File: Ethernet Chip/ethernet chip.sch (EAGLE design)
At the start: 31 parts

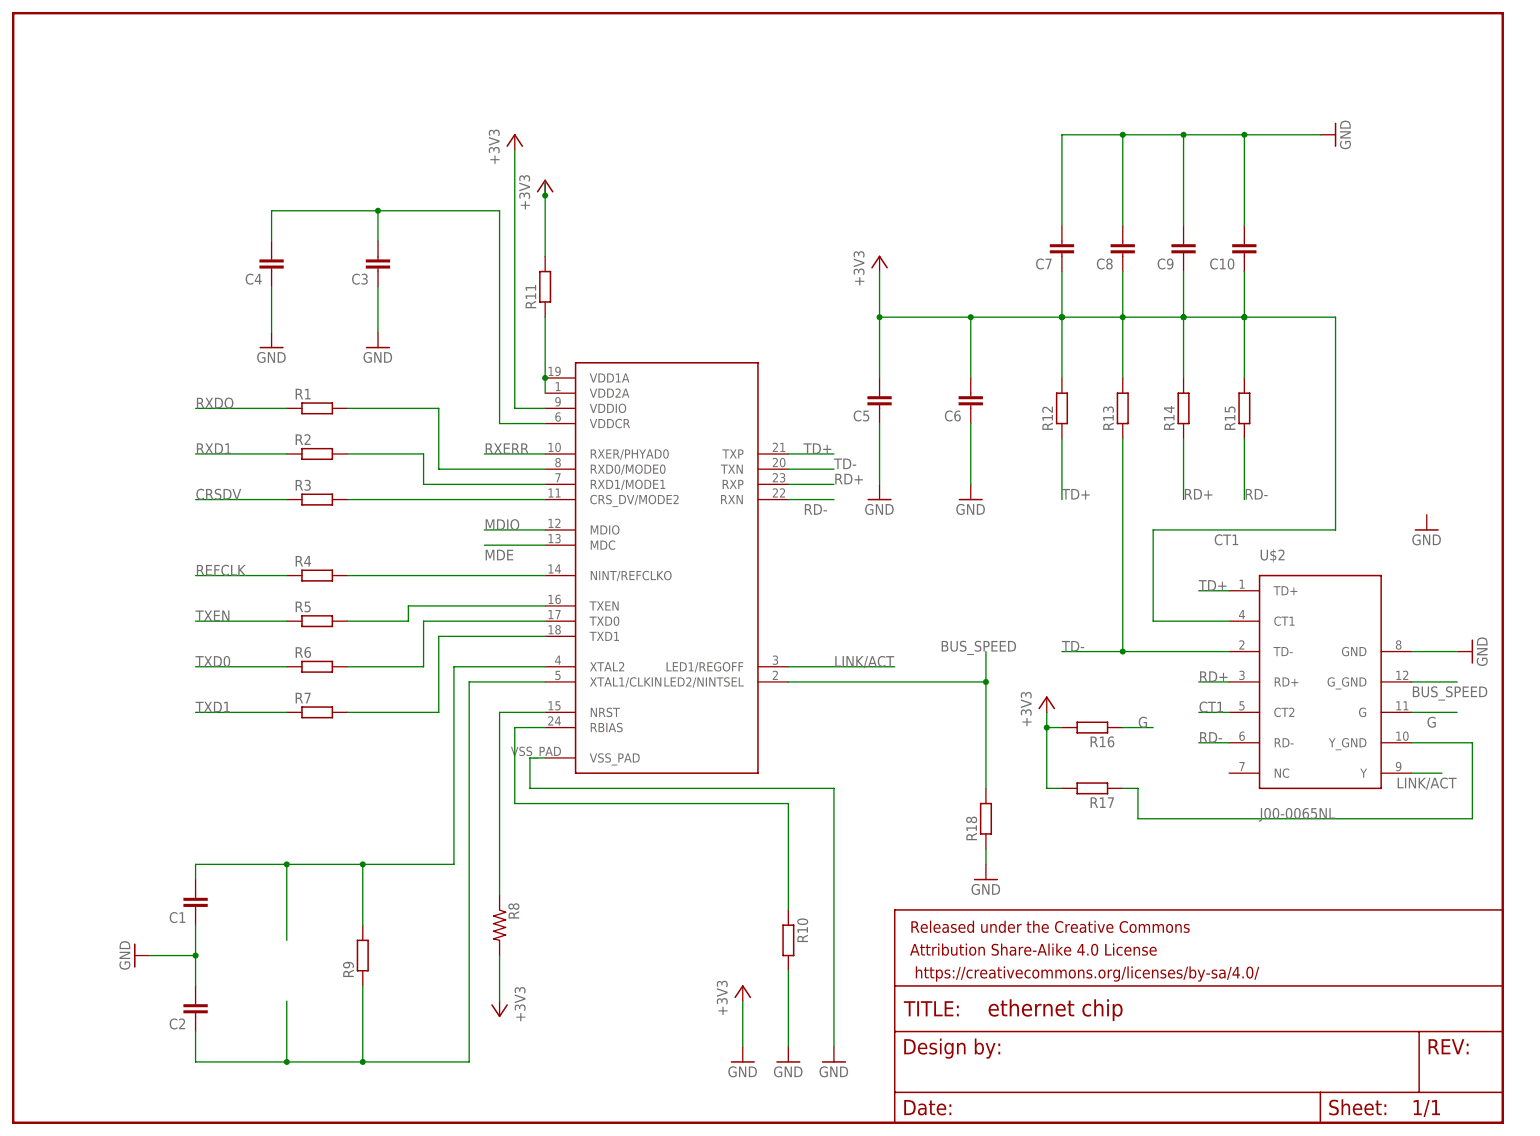
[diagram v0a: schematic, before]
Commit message: Updated Ethernet Schematic (From Paul)
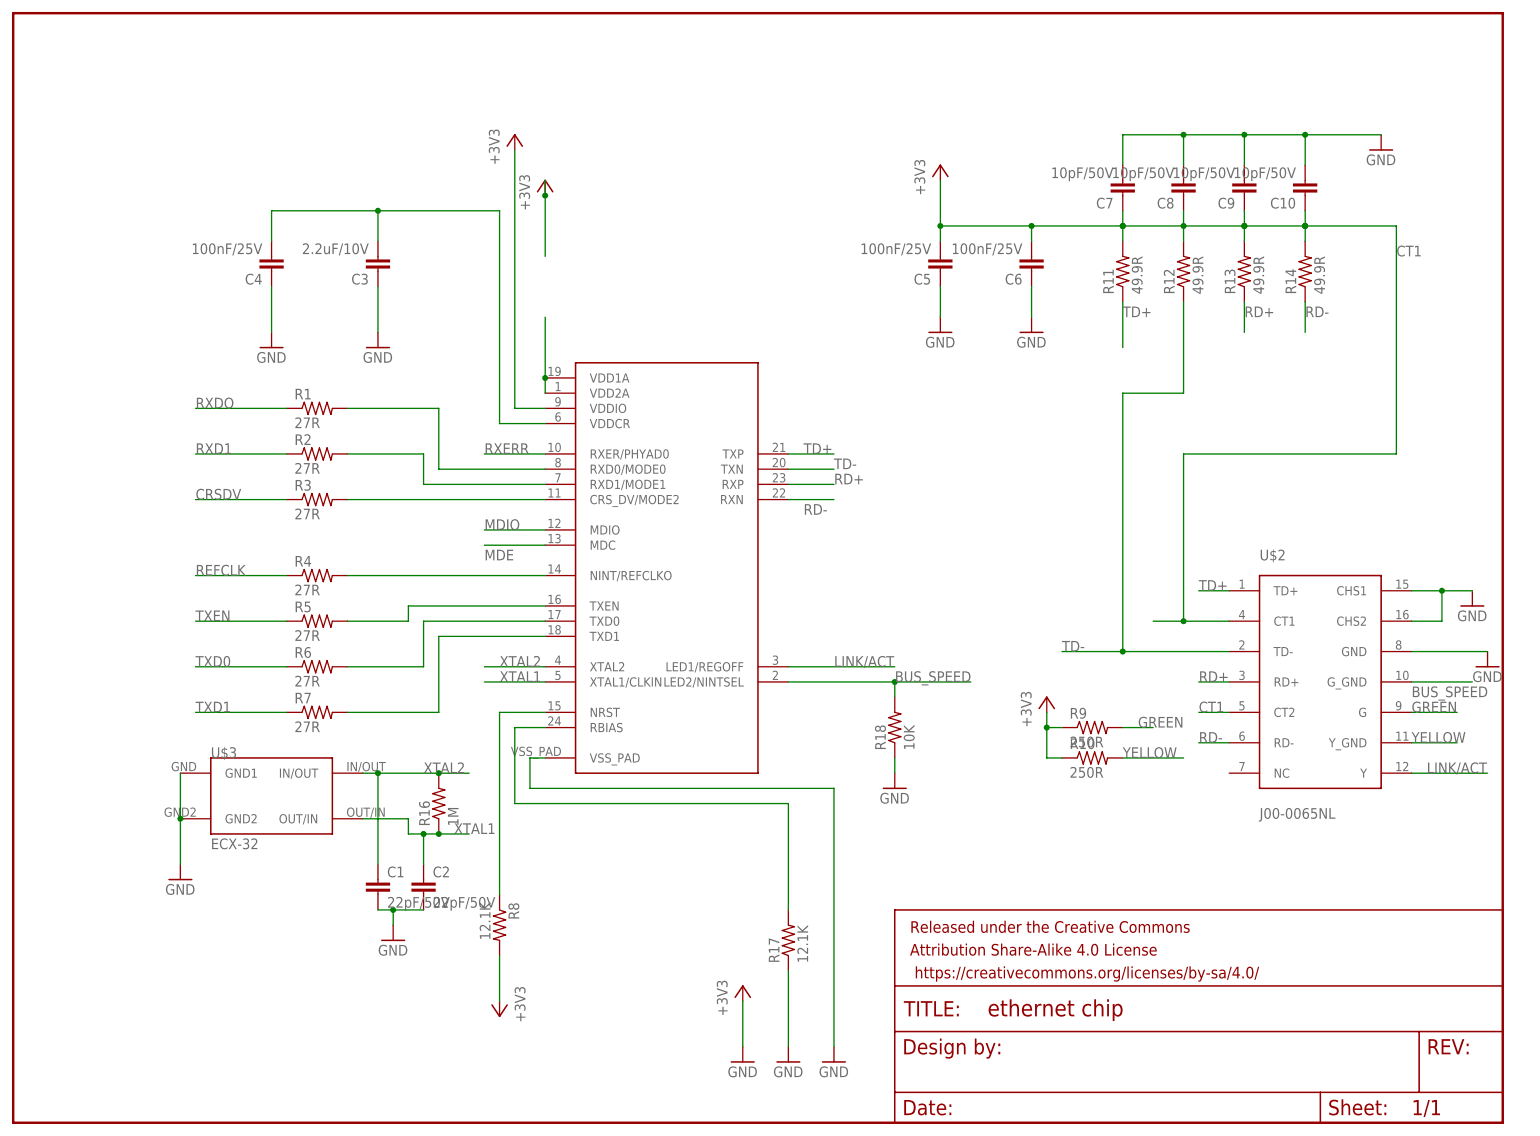
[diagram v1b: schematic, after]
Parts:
- removed R15: (no value), eagle-ltspice:RR0603
- added U$3: ECX-32, Other:ECX-32
- C1, C2: value (none) -> 22pF/50V
- C10, C7, C8, C9: value (none) -> 10pF/50V
- C3: value (none) -> 2.2uF/10V
- C4, C5, C6: value (none) -> 100nF/25V
- R1, R2, R3, R4, R5, R6, R7: value (none) -> 27R; device eagle-ltspice:RR0603 -> resistor:R-US_R0603
- R10, R9: value (none) -> 250R; device eagle-ltspice:RR0603 -> resistor:R-US_R0603
- R11, R12, R13, R14: value (none) -> 49.9R; device eagle-ltspice:RR0603 -> resistor:R-US_R0603
- R16: value (none) -> 1M; device eagle-ltspice:RR0603 -> resistor:R-US_R0603
- R17: value (none) -> 12.1K; device eagle-ltspice:RR0603 -> resistor:R-US_R0603
- R18: value (none) -> 10K; device eagle-ltspice:RR0603 -> resistor:R-US_R0603
- R8: value (none) -> 12.1K
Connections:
- removed net G: R16.1, U$2.G
- removed net N$12: C1.2, R9.2, U$1.XTAL2
- removed net N$13: C2.1, R9.1, U$1.XTAL1/CLKIN
- removed net N$18: R17.1, U$2.Y_GND
- new net GREEN: R9.2, U$2.G
- new net XTAL1: C2.1, R16.1, U$1.XTAL1/CLKIN, U$3.OUT/IN
- new net XTAL2: C1.1, R16.2, U$1.XTAL2, U$3.IN/OUT
- new net YELLOW: R10.2, U$2.Y_GND
- net +3V3: now also R10.1, R9.1; no longer R11.2, R16.2, R17.2
- net CT1: now also R11.2; no longer R15.2
- net GND: now also C1.2, R17.1, U$2.CHS1, U$2.CHS2, U$3.GND1, U$3.GND2; no longer C1.1, R10.2
- net N$11: no longer R11.1
- net N$4: now also R17.2; no longer R10.1
- net RD+: now also R13.1; no longer R14.1
- net RD-: now also R14.1; no longer R15.1
- net TD+: now also R11.1; no longer R12.1
- net TD-: now also R12.1; no longer R13.1
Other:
- moved on the sheet: C1, C10, C2, C5, C6, C7, C8, C9

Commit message: Cleaned up microboard folder
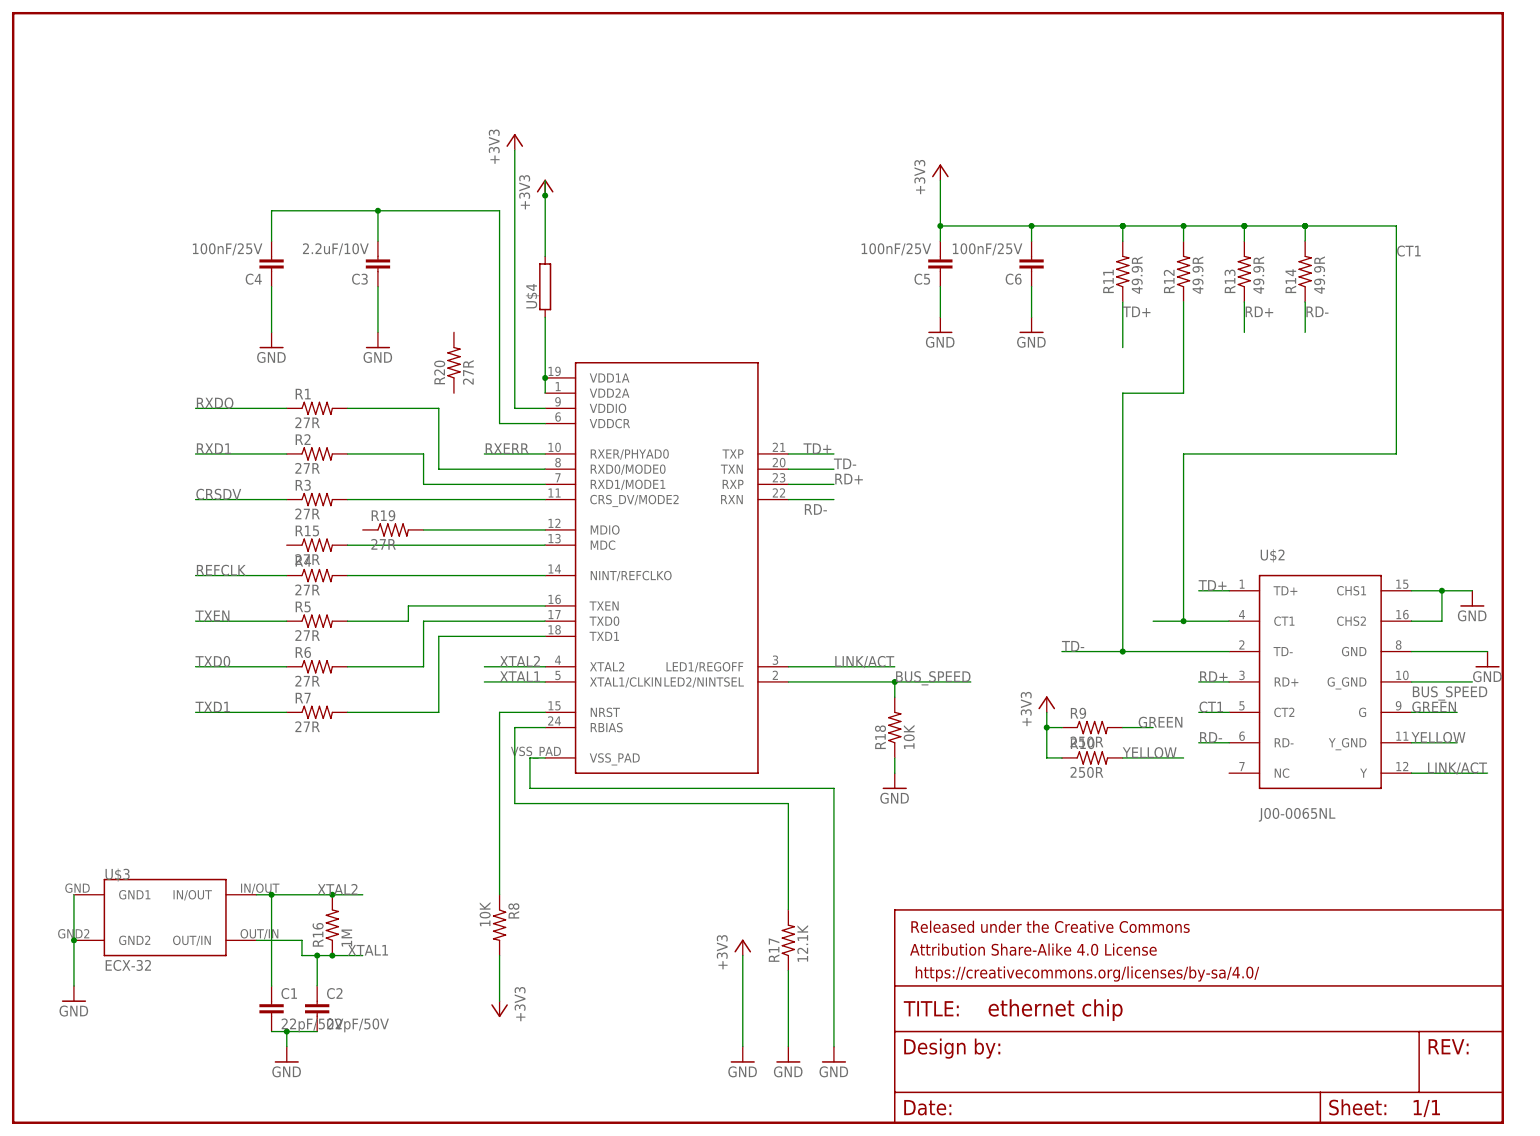
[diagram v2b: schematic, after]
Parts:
- removed C10, C7, C8, C9: 10pF/50V, eagle-ltspice:CC0603
- added R15, R19, R20: 27R, resistor:R-US_R0603
- added U$4: (no value), EthernetChip:553-2382-1-ND
- R8: value 12.1K -> 10K
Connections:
- net +3V3: now also U$4.2
- net CT1: no longer C10.1, C7.1, C8.1, C9.1
- net GND: no longer C10.2, C7.2, C8.2, C9.2
- net MDE: now also R15.2
- net MDIO: now also R19.2
- net N$11: now also U$4.1
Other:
- moved on the sheet: C1, C2, R16, U$3

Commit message: "Cleaned up the ethernet chip schematic"
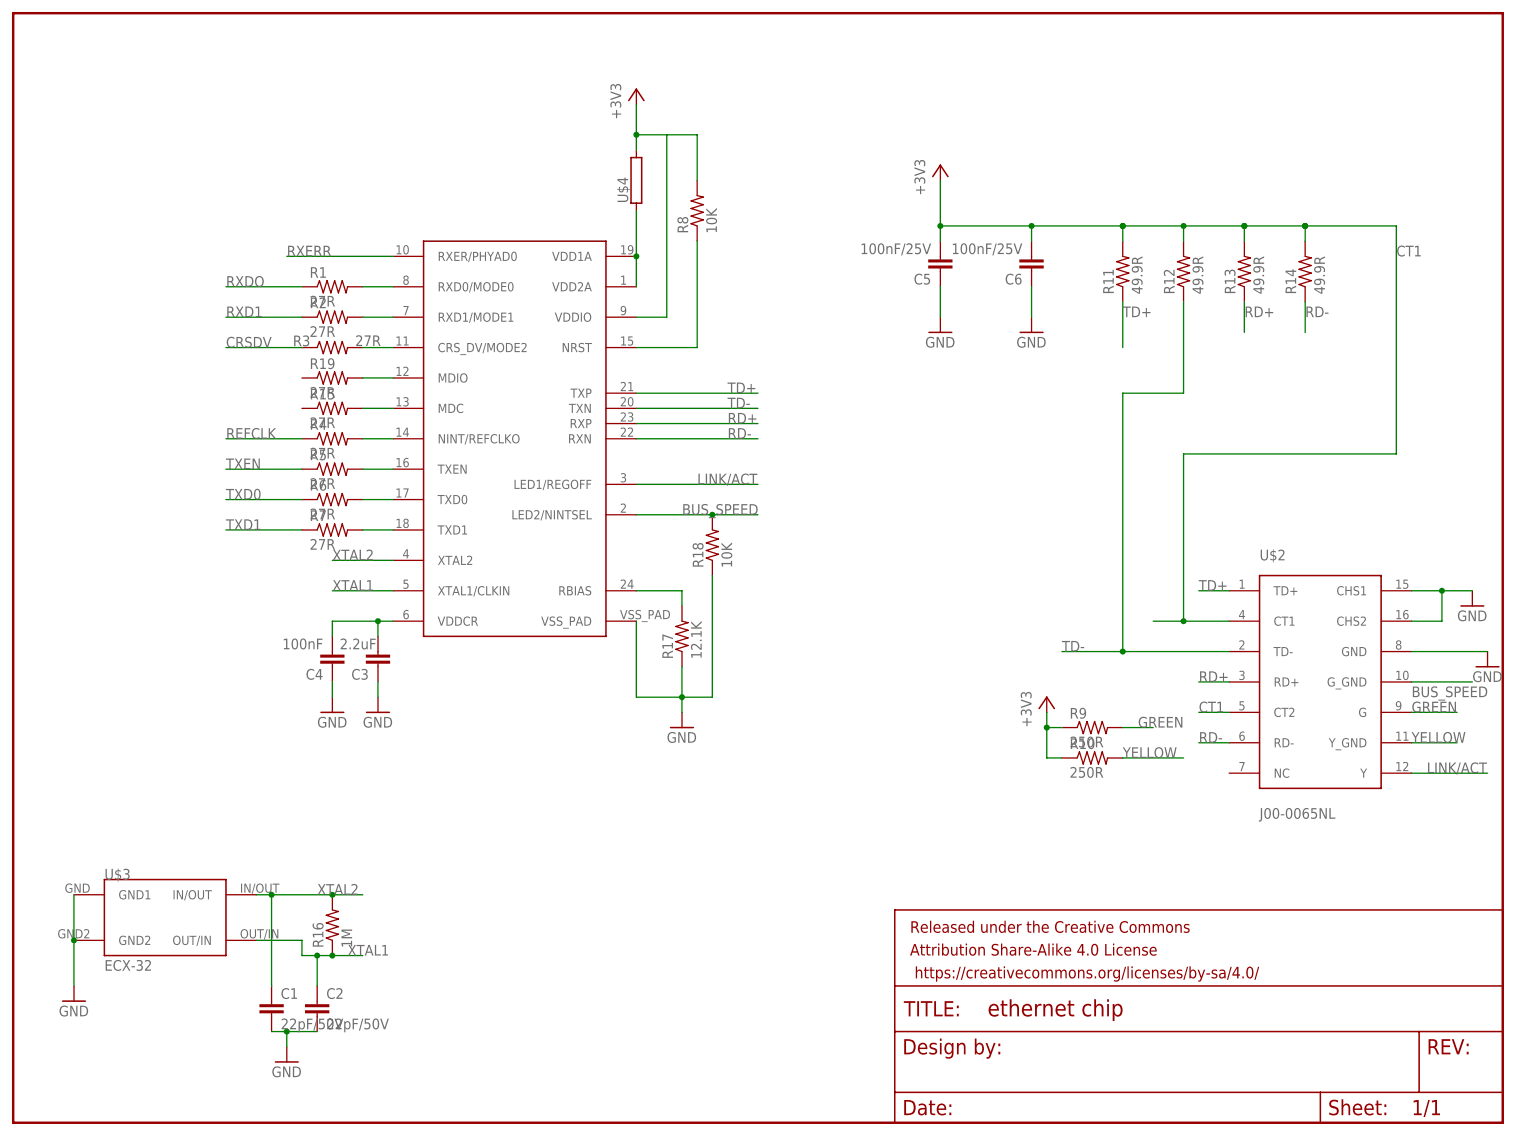
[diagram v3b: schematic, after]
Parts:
- removed R20: 27R, resistor:R-US_R0603
- C3: value 2.2uF/10V -> 2.2uF
- C4: value 100nF/25V -> 100nF
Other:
- moved on the sheet: C3, C4, R1, R15, R17, R18, R19, R2, R3, R4, R5, R6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

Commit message: Finished the ethernet board schematic
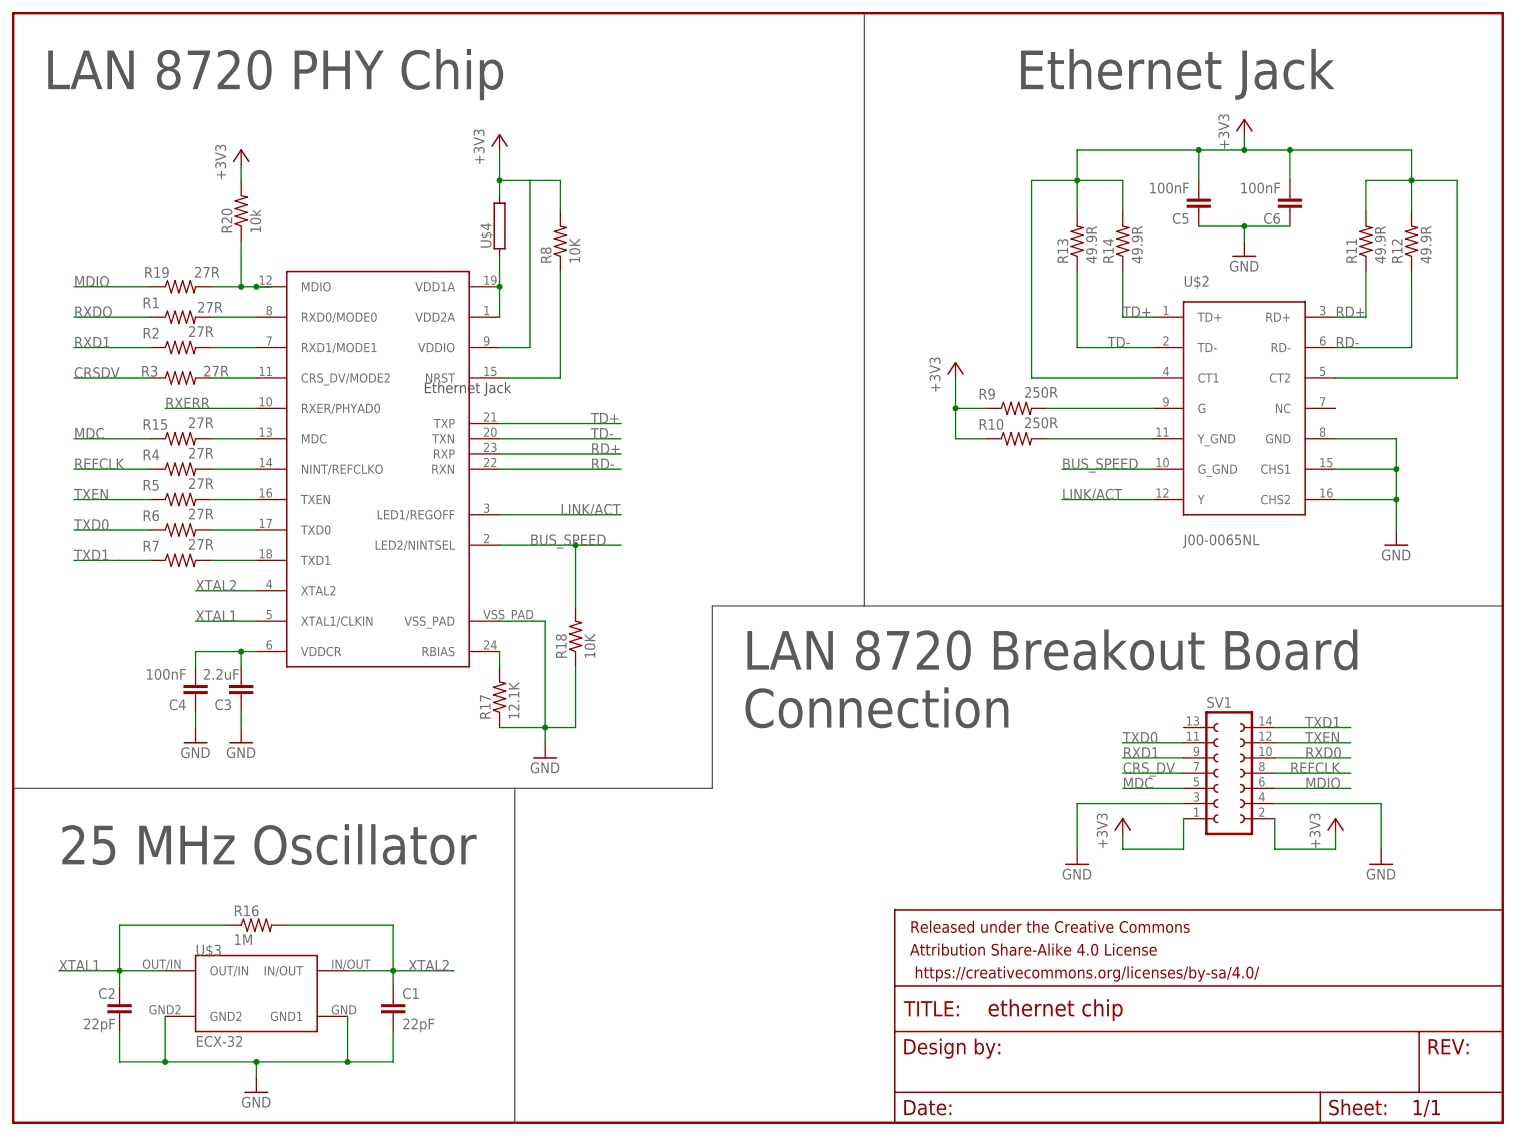
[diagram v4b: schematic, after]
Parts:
- added R20: 10k, resistor:R-US_R0603
- added SV1: (no value), con-lsta:FE07-2
- C1, C2: value 22pF/50V -> 22pF
- C5, C6: value 100nF/25V -> 100nF
- U$1: device Luke:LAN8720LAN8720 -> EthernetChip:LAN8720LAN8720
- U$2: device Paul's Library:J00-0065NL -> EthernetChip:J00-0065NL
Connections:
- removed net CT1: C5.2, C6.2, R11.2, R12.2, R13.2, R14.2, U$2.CT1, U$2.CT2
- new net CRS_DV: SV1.7
- new net MDC: R15.1, SV1.5
- new net N$12: R19.2, R20.1, U$1.MDIO
- new net RXD0: SV1.10
- net +3V3: now also C5.2, C6.2, R11.2, R12.2, R13.2, R14.2, R20.2, SV1.1, SV1.2, U$2.CT1, U$2.CT2
- net GND: now also SV1.3, SV1.4
- net MDIO: now also R19.1, SV1.6; no longer R19.2, U$1.MDIO
- net RD+: now also R11.1; no longer R13.1
- net RD-: now also R12.1; no longer R14.1
- net REFCLK: now also SV1.8
- net RXD1: now also SV1.9
- net TD+: now also R14.1; no longer R11.1
- net TD-: now also R13.1; no longer R12.1
- net TXD0: now also SV1.11
- net TXD1: now also SV1.14
- net TXEN: now also SV1.12
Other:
- note added: "25 MHz Oscillator"
- note added: "Ethernet Jack"
- note added: "LAN 8720 Breakout Board Connection"
- note added: "LAN 8720 PHY Chip"
- moved on the sheet: C1, C2, C3, C4, C5, C6, R1, R10, R11, R12, R13, R14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
